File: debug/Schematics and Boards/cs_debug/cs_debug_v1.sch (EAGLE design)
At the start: 241 parts, among them J1 J-JTAG-CORTEX_SMD, J19 Solar, J2 J-JTAG-CORTEX_SMD, J3 J-JTAG-CORTEX-NEEDLE6-LEGS, J4 J-SERIAL-PORT, J5 J-WURTH-USBC, Q10 2N7002P, Q3 FDN340P, Q4 2N7002P, Q5 FDN340P, Q6 2N7002P, Q7 FDN340P, Q8 2N7002P, Q9 FDN340P, U1 AP2120N-3.3TRG1, U10 OPA357AIDBVTG4, U11 DAC7574IDGS, U12 MCP73871T-2CCI/ML, U13 USB2412-DZK, U14 INA225AIDGK, U15 OPA357AIDBVTG4, U2 TLV1117LV33DCYR, U5 INA225AIDGK, U6 OPA357AIDBVTG4, U7 INA225AIDGK, U8 OPA357AIDBVTG4, U9 INA225AIDGK, Y1 EPSON_TSX-3225_24.0000MF10Z-C3, Y101 32.768kHz, Y102 12mHz-12pF-K7

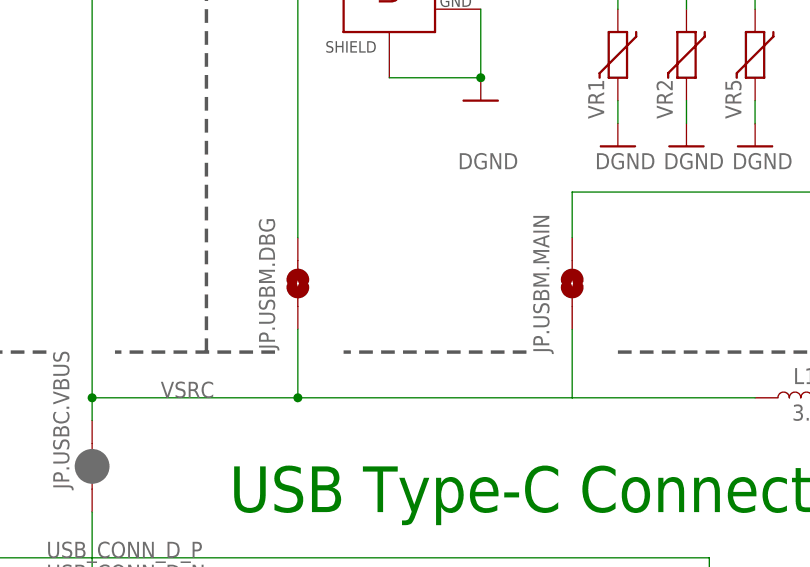
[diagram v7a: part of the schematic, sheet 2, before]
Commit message: DBG-Cleanup Silkscreen
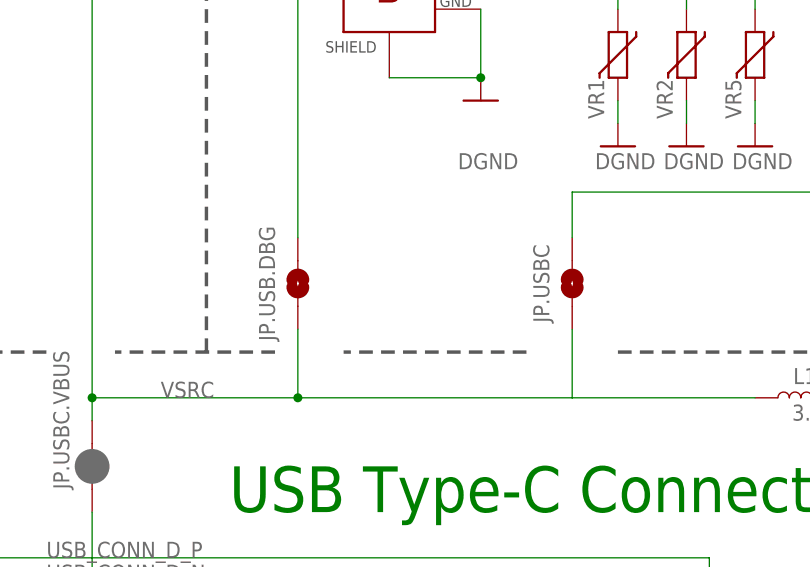
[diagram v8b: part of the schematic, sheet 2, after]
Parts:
- renumbered JP.USBM.DBG to JP.USB.DBG, JP.USBM.MAIN to JP.USBC, J_USB_DBG to J.USB.DBG, J_USB_MAIN to J.USB.MN
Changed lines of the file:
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@@
 <part name="SDA" library="TestPoints" deviceset="TP" device="TP10SQ" package3d_urn="urn:adsk.eagle:package:27962/1"/>
 <part name="D2" library="Diodes" deviceset="BGX50A" device=""/>
-<part name="J_USB_DBG" library="ZX62D-AB-5P8" deviceset="USBABSMTDIP" device="">
+<part name="J.USB.DBG" library="ZX62D-AB-5P8" deviceset="USBABSMTDIP" device="">
 <attribute name="MP" value="ZX62D-AB-5P8(30)"/>
 <attribute name="MPN" value="ZX62D-AB-5P8(30)"/>
@@
 <part name="GND207" library="Supplies" deviceset="GND" device=""/>
 <part name="GND210" library="Supplies" deviceset="GND" device=""/>
-<part name="J_USB_MAIN" library="ZX62D-AB-5P8" deviceset="USBABSMTDIP" device="">
+<part name="J.USB.MN" library="ZX62D-AB-5P8" deviceset="USBABSMTDIP" device="">
 <attribute name="MP" value="ZX62D-AB-5P8(30)"/>
 <attribute name="MPN" value="ZX62D-AB-5P8(30)"/>
@@
 <part name="GND12" library="Supplies" deviceset="GND" device=""/>
 <part name="GND13" library="Supplies" deviceset="GND" device=""/>
-<part name="JP.USBM.MAIN" library="Connectors" deviceset="JUMPER-SMT_2_NO_PASTEFREE" device=""/>
-<part name="JP.USBM.DBG" library="Connectors" deviceset="JUMPER-SMT_2_NO_PASTEFREE" device=""/>
+<part name="JP.USBC" library="Connectors" deviceset="JUMPER-SMT_2_NO_PASTEFREE" device=""/>
+<part name="JP.USB.DBG" library="Connectors" deviceset="JUMPER-SMT_2_NO_PASTEFREE" device=""/>
 <part name="VR1" library="Diodes" deviceset="VARISTOR" device="">
 <attribute name="PART_NO" value="CG0603MLC-05E"/>
@@
 <attribute name="NAME" x="63.50741875" y="342.90741875" size="1.7806" layer="95"/>
 </instance>
-<instance part="J_USB_DBG" gate="G$1" x="162.56" y="403.86" smashed="yes">
+<instance part="J.USB.DBG" gate="G$1" x="162.56" y="403.86" smashed="yes">
 <attribute name="MP" x="162.56" y="403.86" size="1.778" layer="96" display="off"/>
 <attribute name="MPN" x="162.56" y="403.86" size="1.778" layer="96" display="off"/>
@@
 <instance part="GND207" gate="1" x="187.96" y="383.54" smashed="yes"/>
 <instance part="GND210" gate="1" x="203.2" y="383.54" smashed="yes"/>
-<instance part="J_USB_MAIN" gate="G$1" x="223.52" y="386.08" smashed="yes">
+<instance part="J.USB.MN" gate="G$1" x="223.52" y="386.08" smashed="yes">
 <attribute name="MP" x="223.52" y="386.08" size="1.778" layer="96" display="off"/>
 <attribute name="MPN" x="223.52" y="386.08" size="1.778" layer="96" display="off"/>
@@
 <instance part="GND12" gate="1" x="248.92" y="365.76" smashed="yes"/>
 <instance part="GND13" gate="1" x="264.16" y="365.76" smashed="yes"/>
-<instance part="JP.USBM.MAIN" gate="G$1" x="182.88" y="368.3" smashed="yes" rot="R90">
+<instance part="JP.USBC" gate="G$1" x="182.88" y="368.3" smashed="yes" rot="R90">
 <attribute name="NAME" x="180.34" y="368.3" size="1.778" layer="95" font="vector" rot="R90" align="bottom-center"/>
 </instance>
-<instance part="JP.USBM.DBG" gate="G$1" x="152.4" y="368.3" smashed="yes" rot="R90">
+<instance part="JP.USB.DBG" gate="G$1" x="152.4" y="368.3" smashed="yes" rot="R90">
 <attribute name="NAME" x="149.86" y="368.3" size="1.778" layer="95" font="vector" rot="R90" align="bottom-center"/>
 </instance>
@@
 </segment>
 <segment>
-<pinref part="J_USB_DBG" gate="G$1" pin="GND"/>
+<pinref part="J.USB.DBG" gate="G$1" pin="GND"/>
 <pinref part="GND204" gate="1" pin="GND"/>
 <wire x1="172.72" y1="398.78" x2="172.72" y2="391.16" width="0.1524" layer="91"/>
-<pinref part="J_USB_DBG" gate="G$1" pin="SHIELD"/>
+<pinref part="J.USB.DBG" gate="G$1" pin="SHIELD"/>
 <wire x1="162.56" y1="391.16" x2="172.72" y2="391.16" width="0.1524" layer="91"/>
 <junction x="172.72" y="391.16"/>
@@
 </segment>
 <segment>
-<pinref part="J_USB_MAIN" gate="G$1" pin="GND"/>
+<pinref part="J.USB.MN" gate="G$1" pin="GND"/>
 <pinref part="GND9" gate="1" pin="GND"/>
 <wire x1="233.68" y1="381" x2="233.68" y2="373.38" width="0.1524" layer="91"/>
-<pinref part="J_USB_MAIN" gate="G$1" pin="SHIELD"/>
+<pinref part="J.USB.MN" gate="G$1" pin="SHIELD"/>
 <wire x1="223.52" y1="373.38" x2="233.68" y2="373.38" width="0.1524" layer="91"/>
 <junction x="233.68" y="373.38"/>
@@
 <net name="USB_BKUP_MAIN_OTGID" class="0">
 <segment>
-<pinref part="J_USB_MAIN" gate="G$1" pin="USBID"/>
+<pinref part="J.USB.MN" gate="G$1" pin="USBID"/>
 <wire x1="233.68" y1="383.54" x2="248.92" y2="383.54" width="0.1524" layer="91"/>
 <label x="269.24" y="383.54" size="1.016" layer="95" xref="yes"/>
@@
 <net name="USB_BKUP_MAIN_D_N" class="0">
 <segment>
-<pinref part="J_USB_MAIN" gate="G$1" pin="D-"/>
+<pinref part="J.USB.MN" gate="G$1" pin="D-"/>
 <wire x1="233.68" y1="388.62" x2="264.16" y2="388.62" width="0.1524" layer="91"/>
 <wire x1="264.16" y1="381" x2="264.16" y2="388.62" width="0.1524" layer="91"/>
@@
 <net name="USB_BKUP_MAIN_D_P" class="0">
 <segment>
-<pinref part="J_USB_MAIN" gate="G$1" pin="D+"/>
+<pinref part="J.USB.MN" gate="G$1" pin="D+"/>
 <wire x1="233.68" y1="386.08" x2="256.54" y2="386.08" width="0.1524" layer="91"/>
 <wire x1="256.54" y1="381" x2="256.54" y2="386.08" width="0.1524" layer="91"/>
@@
 <net name="USB_BKUP_DBG_VBUS" class="1">
 <segment>
-<pinref part="J_USB_DBG" gate="G$1" pin="VBUS"/>
+<pinref part="J.USB.DBG" gate="G$1" pin="VBUS"/>
 <wire x1="172.72" y1="408.94" x2="175.26" y2="408.94" width="0.1524" layer="91"/>
 <wire x1="175.26" y1="408.94" x2="175.26" y2="414.02" width="0.1524" layer="91"/>
 <wire x1="175.26" y1="414.02" x2="152.4" y2="414.02" width="0.1524" layer="91"/>
 <wire x1="152.4" y1="414.02" x2="152.4" y2="373.38" width="0.1524" layer="91"/>
-<pinref part="JP.USBM.DBG" gate="G$1" pin="2"/>
+<pinref part="JP.USB.DBG" gate="G$1" pin="2"/>
 <label x="152.4" y="414.02" size="1.778" layer="95"/>
 </segment>
@@
 <net name="USB_BKUP_MAIN_VBUS" class="1">
 <segment>
-<pinref part="J_USB_MAIN" gate="G$1" pin="VBUS"/>
+<pinref part="J.USB.MN" gate="G$1" pin="VBUS"/>
 <wire x1="233.68" y1="391.16" x2="241.3" y2="391.16" width="0.1524" layer="91"/>
 <wire x1="241.3" y1="391.16" x2="241.3" y2="396.24" width="0.1524" layer="91"/>
@@
 <wire x1="213.36" y1="378.46" x2="182.88" y2="378.46" width="0.1524" layer="91"/>
 <wire x1="182.88" y1="378.46" x2="182.88" y2="373.38" width="0.1524" layer="91"/>
-<pinref part="JP.USBM.MAIN" gate="G$1" pin="2"/>
+<pinref part="JP.USBC" gate="G$1" pin="2"/>
 <label x="213.36" y="396.24" size="1.778" layer="95"/>
 </segment>
@@
 <net name="USB_BKUP_DBG_D_N" class="0">
 <segment>
-<pinref part="J_USB_DBG" gate="G$1" pin="D-"/>
+<pinref part="J.USB.DBG" gate="G$1" pin="D-"/>
 <wire x1="172.72" y1="406.4" x2="203.2" y2="406.4" width="0.1524" layer="91"/>
 <wire x1="203.2" y1="398.78" x2="203.2" y2="406.4" width="0.1524" layer="91"/>
@@
 <net name="USB_BKUP_DBG_D_P" class="0">
 <segment>
-<pinref part="J_USB_DBG" gate="G$1" pin="D+"/>
+<pinref part="J.USB.DBG" gate="G$1" pin="D+"/>
 <wire x1="172.72" y1="403.86" x2="195.58" y2="403.86" width="0.1524" layer="91"/>
 <wire x1="195.58" y1="398.78" x2="195.58" y2="403.86" width="0.1524" layer="91"/>
@@
 <net name="USB_BKUP_DBG_OTGID" class="0">
 <segment>
-<pinref part="J_USB_DBG" gate="G$1" pin="USBID"/>
+<pinref part="J.USB.DBG" gate="G$1" pin="USBID"/>
 <wire x1="172.72" y1="401.32" x2="187.96" y2="401.32" width="0.1524" layer="91"/>
 <label x="208.28" y="401.32" size="1.016" layer="95" xref="yes"/>
@@
 <wire x1="129.54" y1="421.64" x2="132.08" y2="424.18" width="0.1524" layer="91"/>
 <pinref part="JP.USBC.VBUS" gate="G$1" pin="2"/>
-<pinref part="JP.USBM.MAIN" gate="G$1" pin="1"/>
+<pinref part="JP.USBC" gate="G$1" pin="1"/>
 <wire x1="182.88" y1="363.22" x2="182.88" y2="355.6" width="0.1524" layer="91"/>
-<pinref part="JP.USBM.DBG" gate="G$1" pin="1"/>
+<pinref part="JP.USB.DBG" gate="G$1" pin="1"/>
 <wire x1="152.4" y1="363.22" x2="152.4" y2="355.6" width="0.1524" layer="91"/>
 <junction x="152.4" y="355.6"/>
